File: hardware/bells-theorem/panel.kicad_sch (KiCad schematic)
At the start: 79 parts, among them J10 D, J11 C, J12 DA, J13 CD, J14 DAB, J15 CDA, J16 A, J17 B, J18 AB, J19 BC, J20 ABC, J21 BCD, J22 left, J23 right, J4 IN, J5 CVA, J6 CVB, J7 CVC, J8 CVD, J9 ABCD, Q11 2N3904, Q2 2N3904, Q5 2N3904, Q8 2N3904

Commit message: All changes up to date with latest revisions
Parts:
- C40, C41, C42, C43, C44, C45, C46, C47, C48: footprint Capacitor_SMD:C_0805_2012Metric_Pad1.15x1.40mm_HandSolder -> Capacitor_SMD:C_0805_2012Metric_Pad1.18x1.45mm_HandSolder
- R1, R100, R101, R102, R103, R104, R105, R131, R132, R133, R134, R135, R136, R137, R138, R139, R140, R2, R3, R4, R5, R6, R7, R8, R9, R92, R93, R94, R95, R96, R97, R98, R99: footprint Resistor_SMD:R_0805_2012Metric_Pad1.15x1.40mm_HandSolder -> Resistor_SMD:R_0805_2012Metric_Pad1.20x1.40mm_HandSolder
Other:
- title: (none) -> Bell's Theorem

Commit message: last hardware / software updates
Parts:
- removed Q11, Q2, Q5, Q8: 2N3904, Package_TO_SOT_SMD:SOT-23_Handsoldering, symbol Device:Q_NPN_BEC
- removed R100, R101, R7, R8: 360R, Resistor_SMD:R_0805_2012Metric_Pad1.20x1.40mm_HandSolder, symbol Device:R_US
- removed R102, R103, R92, R93: 15K, Resistor_SMD:R_0805_2012Metric_Pad1.20x1.40mm_HandSolder, symbol Device:R_US
- removed R105, R131, R133, R134, R137, R138, R139, R140: 270R, Resistor_SMD:R_0805_2012Metric_Pad1.20x1.40mm_HandSolder, symbol Device:R_US
- added C30, C31, C32, C6: 100nF, Capacitor_SMD:C_0805_2012Metric_Pad1.18x1.45mm_HandSolder, symbol Device:C_Small
- added R100, R19, R21, R92: 100R, Resistor_SMD:R_0805_2012Metric_Pad1.20x1.40mm_HandSolder, symbol Device:R_Small_US
- added R22, R24, R25, R27, R28, R30, R31, R33, R34, R7, R8, R93: 33R, Resistor_SMD:R_0805_2012Metric_Pad1.20x1.40mm_HandSolder, symbol Device:R_Small_US
- added U14, U15, U16, U17: WS2811, Package_SO:SOIC-8_3.9x4.9mm_P1.27mm, symbol Driver_LED:WS2811
- R104, R132, R135, R136: value 15K -> 3.3K
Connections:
- net +5V: now also S1.5 (+), S2.5 (+), S3.5 (+), S4.5 (+), R100.1, R19.1, R21.1, R92.1
- net GND: now also C30.2, C31.2, C32.2, C6.2, U14.4 (GND), U15.4 (GND), U16.4 (GND), U17.4 (GND)
- net at S1.2 (-G): now also U14.2 (OUTG)
- net at S1.4 (-B): now also U14.3 (OUTB)
- net at S1.1 (-R): now also U14.1 (OUTR)
- net at S3.1 (-R): now also U16.1 (OUTR)
- net at S3.2 (-G): now also U16.2 (OUTG)
- net at S3.4 (-B): now also U16.3 (OUTB)
- net at S4.1 (-R): now also U17.1 (OUTR)
- net at S4.2 (-G): now also U17.2 (OUTG)
- net at S4.4 (-B): now also U17.3 (OUTB)
- net at S2.1 (-R): now also U15.1 (OUTR)
- net at S2.2 (-G): now also U15.2 (OUTG)
- net at S2.4 (-B): now also U15.3 (OUTB)
- net at D6.1 (DOUT): now also R30.1; no longer D9.4 (DIN)
- net at D6.4 (DIN): now also R27.1; no longer D7.1 (DOUT)
- net at D7.4 (DIN): now also R28.1; no longer D8.1 (DOUT)
- net at D8.4 (DIN): now also R24.1; no longer D5.1 (DOUT)
- net at D4.1 (DOUT): now also R22.1; no longer D5.4 (DIN)
- net at D4.4 (DIN): now also R8.1; no longer D3.1 (DOUT)
- net at D3.4 (DIN): now also R7.2; no longer R9.2
- net at D9.1 (DOUT): now also R31.1; no longer D10.4 (DIN)
- net at D10.1 (DOUT): now also R33.1; no longer D11.4 (DIN)
- net at D11.1 (DOUT): now also R93.2
- removed net +12V: J22.18 (Pin_18), J4.2, S1.5 (+), S2.5 (+), S3.5 (+), S4.5 (+)
- new net: D7.1 (DOUT), R27.2
- new net: D8.1 (DOUT), R28.2
- new net: D5.1 (DOUT), R25.2
- new net: D5.4 (DIN), R22.2
- new net: D3.1 (DOUT), R8.2
- new net: D9.4 (DIN), R30.2
- new net: D10.4 (DIN), R31.2
- new net: D11.4 (DIN), R34.1
- new net: R9.2, U14.6 (DIN)
- new net: R93.1, U16.6 (DIN)
- new net: C30.1, R92.2, U16.8 (VDD)
- new net: C31.1, R100.2, U17.8 (VDD)
- new net: R7.1, U14.5 (DO)
- new net: C6.1, R19.2, U14.8 (VDD)
- new net: R24.2, U15.5 (DO)
- new net: R25.1, U15.6 (DIN)
- new net: C32.1, R21.2, U15.8 (VDD)
- new net: R34.2, U17.5 (DO)
- new net: R33.2, U17.6 (DIN)
- new net +10V: J22.18 (Pin_18), J4.2
- no-connect marks 14 -> 18
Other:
- note removed: "can’t tie all anodes and all cathodes together!"
- moved on the sheet: C40, C41, C42, C43, C44, C45, C46, C47, C48, D10, D11, D3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

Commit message: version 0.6 hardware and code
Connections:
- net at D8.4 (DIN): now also R25.1; no longer R24.1
- net at D3.4 (DIN): now also R9.2; no longer R7.2
- net at D10.1 (DOUT): now also R34.2; no longer R33.1
- net at U14.6 (DIN): now also R7.1; no longer R9.2
- net at U16.5 (DO): now also R33.1
- net at U14.5 (DO): no longer R7.1
- net at U15.5 (DO): now also R7.2; no longer R24.2
- net at U15.6 (DIN): now also R24.2; no longer R25.1
- net at U17.5 (DO): now also R24.1; no longer R34.2
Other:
- note added: "all the LEDs have to come before the WS2811 chips; in some cases the LEDs won't work if they are downstream of the chips"
- moved on the sheet: R24, R9

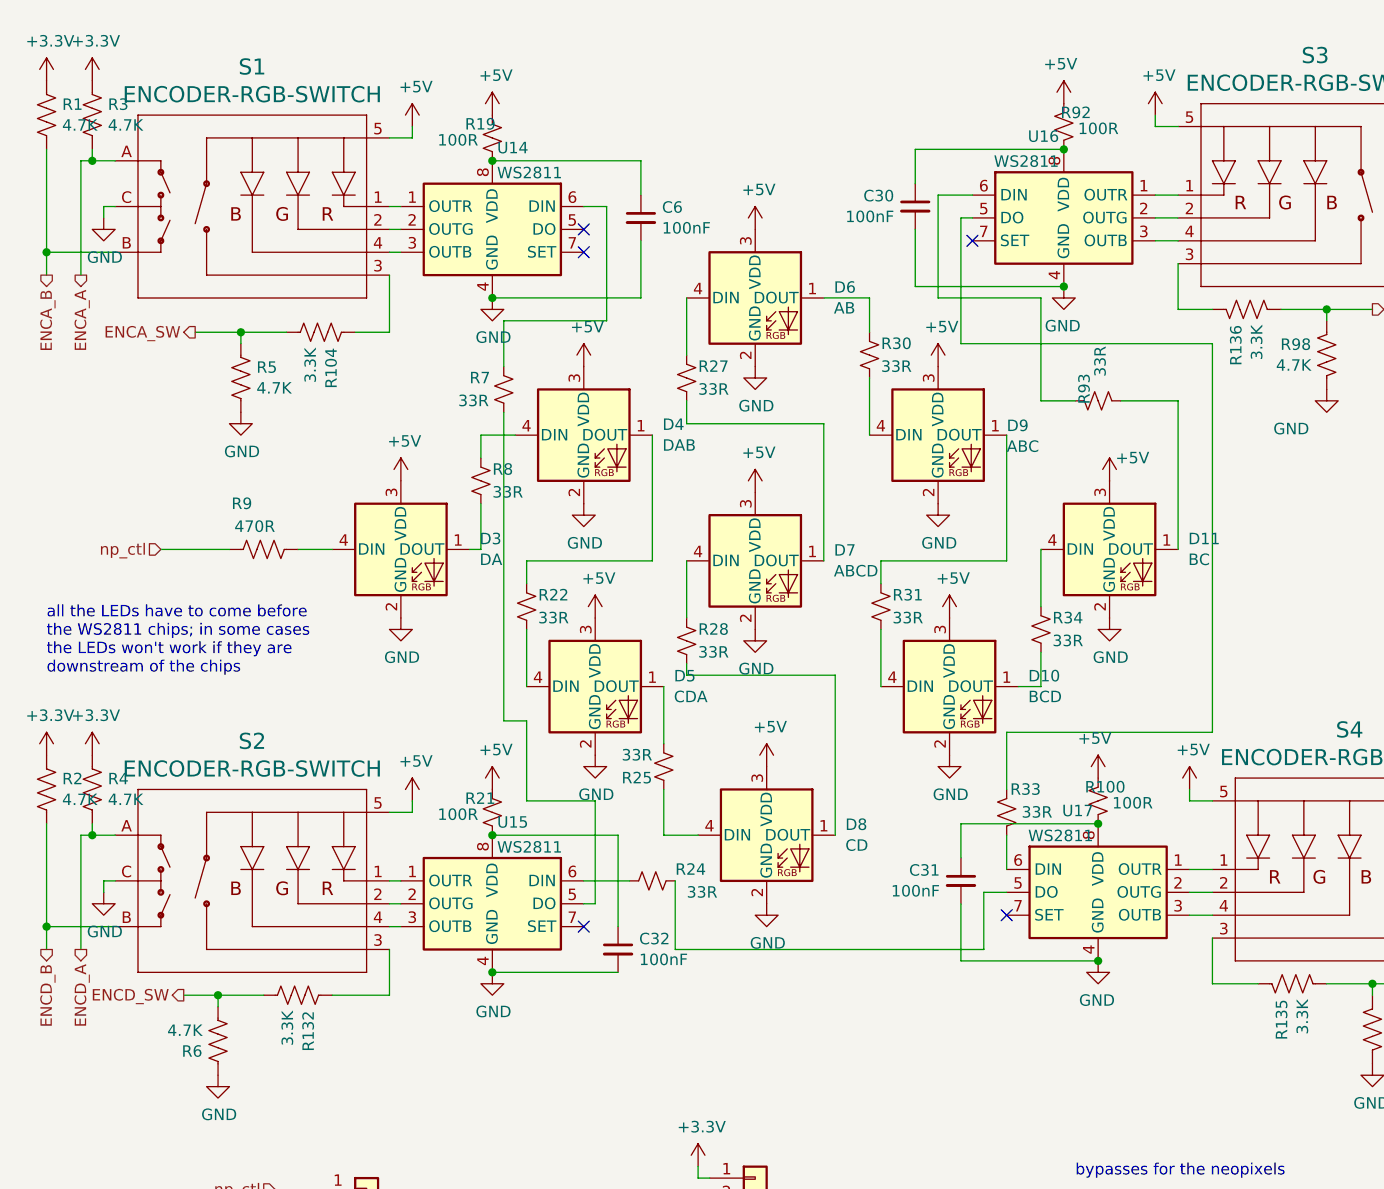
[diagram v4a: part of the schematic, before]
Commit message: current revision actually 0.6 was 1.0 candidate, but needs major revision
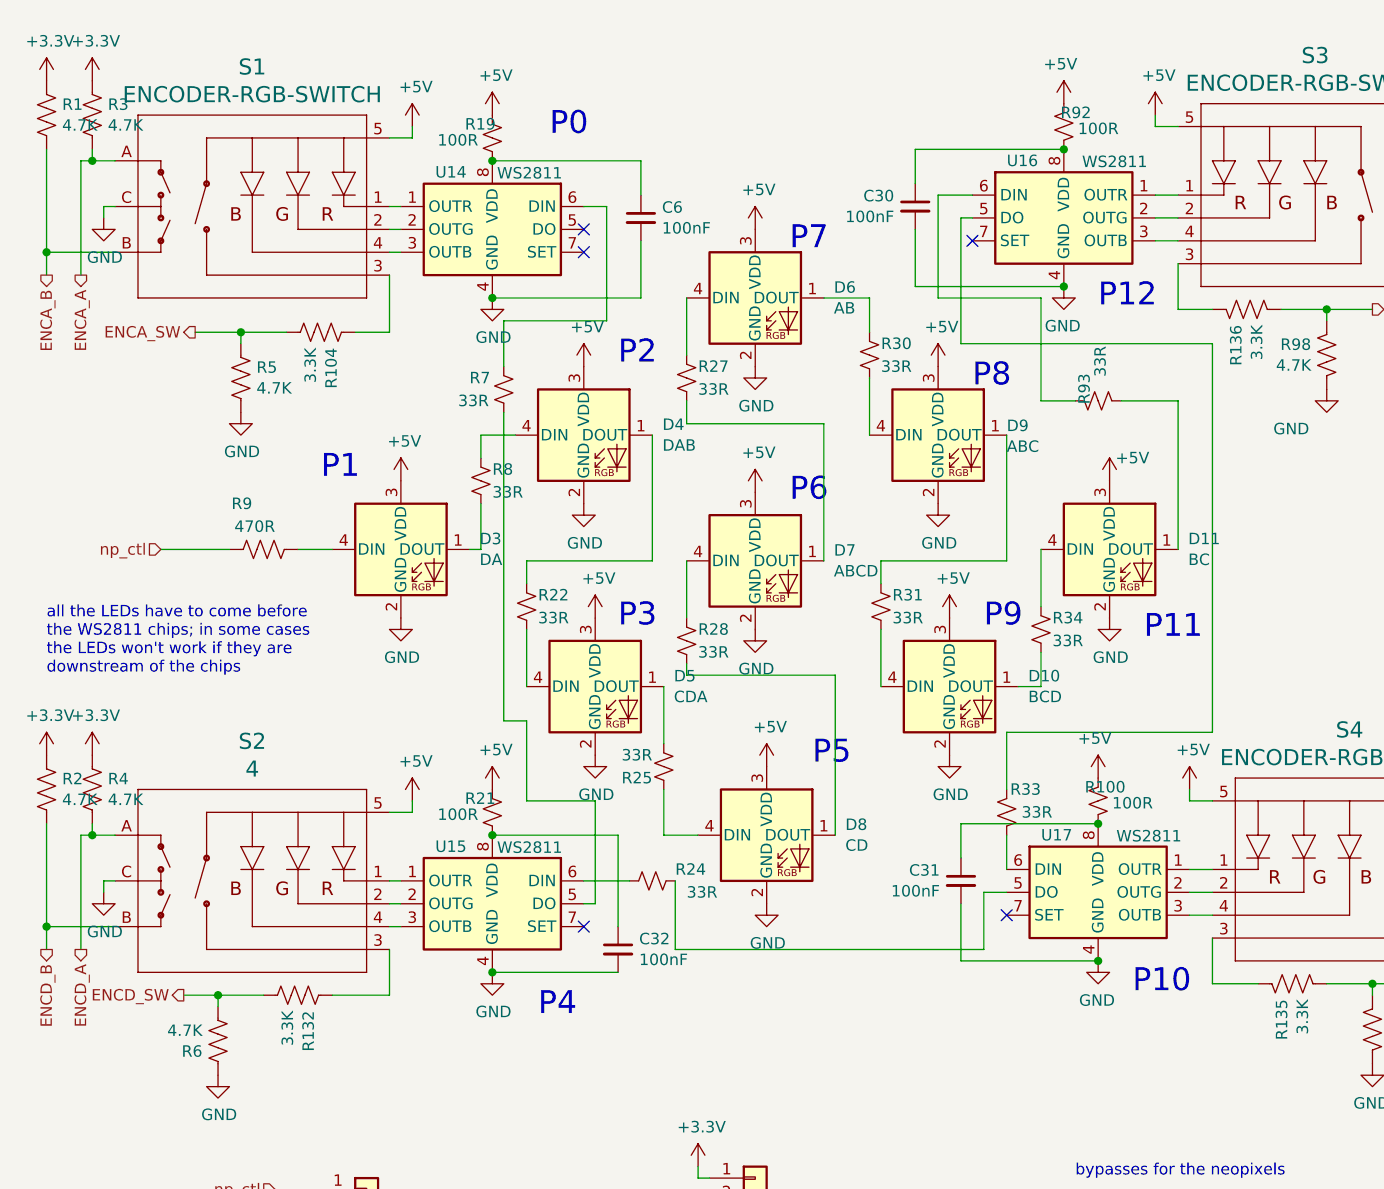
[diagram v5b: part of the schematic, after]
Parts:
- D10, D11, D3, D4, D5, D6, D7, D8, D9: footprint LED_THT:LED_D5.0mm-4_RGB_Wide_Pins -> LED_THT:LED_D5.0mm-4_RGB
- S2: value ENCODER-RGB-SWITCH -> 4
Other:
- note added: "P0"
- note added: "P1"
- note added: "P10"
- note added: "P11"
- note added: "P12"
- note added: "P2"
- note added: "P3"
- note added: "P4"
- note added: "P5"
- note added: "P6"
- note added: "P7"
- note added: "P8"
- note added: "P9"

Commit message: checking in old outstanding changes prior to debugging with Claude Code
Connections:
- net +10V is gone; now on net +5V: J22.18 (Pin_18), J4.2
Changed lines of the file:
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@@
     (pin "9")
-  )
-  (symbol (lib_id "power:+10V") (at 34.29 184.15 0) (unit 1)
-    (in_bom yes) (on_board yes) (fields_autoplaced)
-    (property "Reference" "#PWR043" (id 0) (at 34.29 187.96 0)
-      (effects (font (size 1.27 1.27)) hide)
-    )
-    (property "Value" "+10V" (id 1) (at 34.29 180.5455 0))
-    (property "Footprint" "" (id 2) (at 34.29 184.15 0)
-      (effects (font (size 1.27 1.27)) hide)
-    )
-    (property "Datasheet" "" (id 3) (at 34.29 184.15 0)
-      (effects (font (size 1.27 1.27)) hide)
-    )
-    (pin "1")
   )
   (symbol (lib_id "Driver_LED:WS2811") (at 129.54 34.29 0) (unit 1)
@@
     (pin "1")
   )
-  (symbol (lib_id "power:+10V") (at 196.85 105.41 0) (unit 1)
-    (in_bom yes) (on_board yes) (fields_autoplaced)
-    (property "Reference" "#PWR092" (id 0) (at 196.85 109.22 0)
-      (effects (font (size 1.27 1.27)) hide)
-    )
-    (property "Value" "+10V" (id 1) (at 196.85 101.8055 0))
-    (property "Footprint" "" (id 2) (at 196.85 105.41 0)
-      (effects (font (size 1.27 1.27)) hide)
-    )
-    (property "Datasheet" "" (id 3) (at 196.85 105.41 0)
-      (effects (font (size 1.27 1.27)) hide)
-    )
-    (pin "1")
-  )
   (symbol (lib_id "power:+5V") (at 66.04 97.79 0) (unit 1)
     (in_bom yes) (on_board yes)
@@
     (pin "2")
   )
+  (symbol (lib_id "power:+5V") (at 196.85 105.41 0) (unit 1)
+    (in_bom yes) (on_board yes)
+    (property "Reference" "#PWR0130" (id 0) (at 196.85 109.22 0)
+      (effects (font (size 1.27 1.27)) hide)
+    )
+    (property "Value" "+5V" (id 1) (at 197.231 101.0158 0))
+    (property "Footprint" "" (id 2) (at 196.85 105.41 0)
+      (effects (font (size 1.27 1.27)) hide)
+    )
+    (property "Datasheet" "" (id 3) (at 196.85 105.41 0)
+      (effects (font (size 1.27 1.27)) hide)
+    )
+    (pin "1")
+  )
   (symbol (lib_id "Device:C_Small") (at 113.03 33.02 0) (mirror y) (unit 1)
     (in_bom yes) (on_board yes)
@@
     (pin "2")
   )
+  (symbol (lib_id "power:+5V") (at 34.29 184.15 0) (unit 1)
+    (in_bom yes) (on_board yes)
+    (property "Reference" "#PWR0129" (id 0) (at 34.29 187.96 0)
+      (effects (font (size 1.27 1.27)) hide)
+    )
+    (property "Value" "+5V" (id 1) (at 34.671 179.7558 0))
+    (property "Footprint" "" (id 2) (at 34.29 184.15 0)
+      (effects (font (size 1.27 1.27)) hide)
+    )
+    (property "Datasheet" "" (id 3) (at 34.29 184.15 0)
+      (effects (font (size 1.27 1.27)) hide)
+    )
+    (pin "1")
+  )
   (symbol (lib_id "Device:R_Small_US") (at 87.63 52.07 0) (unit 1)
